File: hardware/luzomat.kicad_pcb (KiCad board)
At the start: 4 copper layers, 187 x 103 mm, 126 parts, among them J1 Screw_Terminal_01x02, J10 Screw_Terminal_01x02, J11 Screw_Terminal_01x02, J12 Screw_Terminal_01x02, J13 Screw_Terminal_01x02, J14 Screw_Terminal_01x02, J15 Screw_Terminal_01x02, J16 Screw_Terminal_01x02, J17 Screw_Terminal_01x02, J18 Screw_Terminal_01x02, J19 Screw_Terminal_01x02, J2 Screw_Terminal_01x02, J20 Screw_Terminal_01x02, J21 Screw_Terminal_01x02, J3 40HAT, J5 Screw_Terminal_01x02, J6 Screw_Terminal_01x02, J7 Screw_Terminal_01x02, J8 Screw_Terminal_01x02, J9 Screw_Terminal_01x02, K1 G5Q-1, K2 G5Q-1, K3 G5Q-1, K4 G5Q-1, K5 G5Q-1, K6 G5Q-1, Q1 DMG2305UX-13, Q10 2N7002, Q11 2N7002, Q12 2N7002, Q13 2N7002, Q2 2N7002, Q3 DMG2305UX-13, Q4 2N7002, Q5 2N7002, Q6 2N7002, Q7 2N7002, Q8 2N7002, Q9 2N7002, U1 CAT24C256, U2 LM1085-3.3, U3 MAX31856, U4 MAX31856, U5 SN74LVC1G123DCTR, U6 SN74LVC1T45DBV

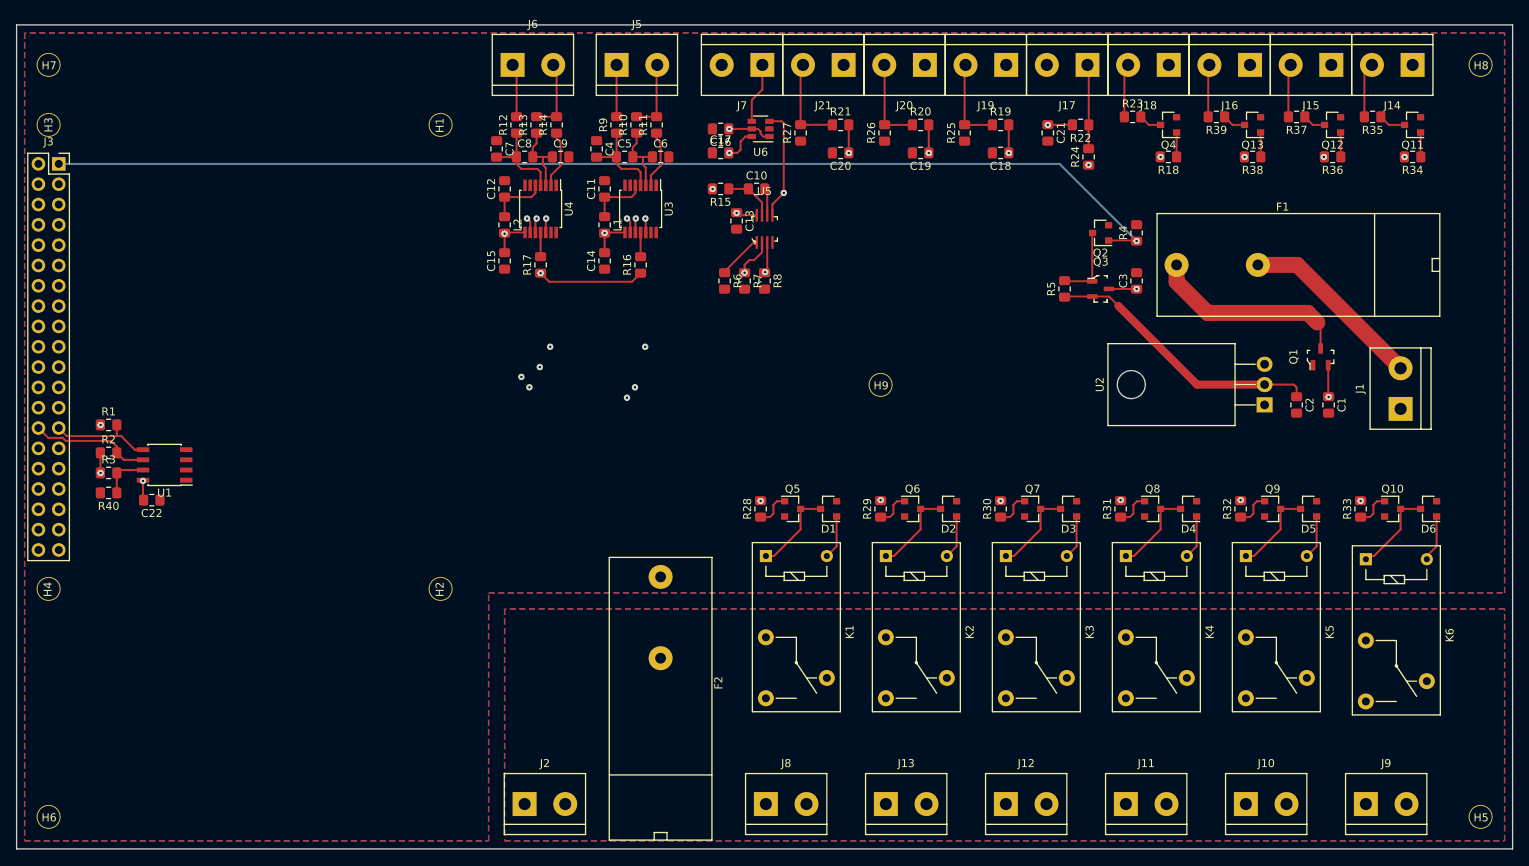
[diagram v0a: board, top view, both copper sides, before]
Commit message: added testpoints and silkscreen
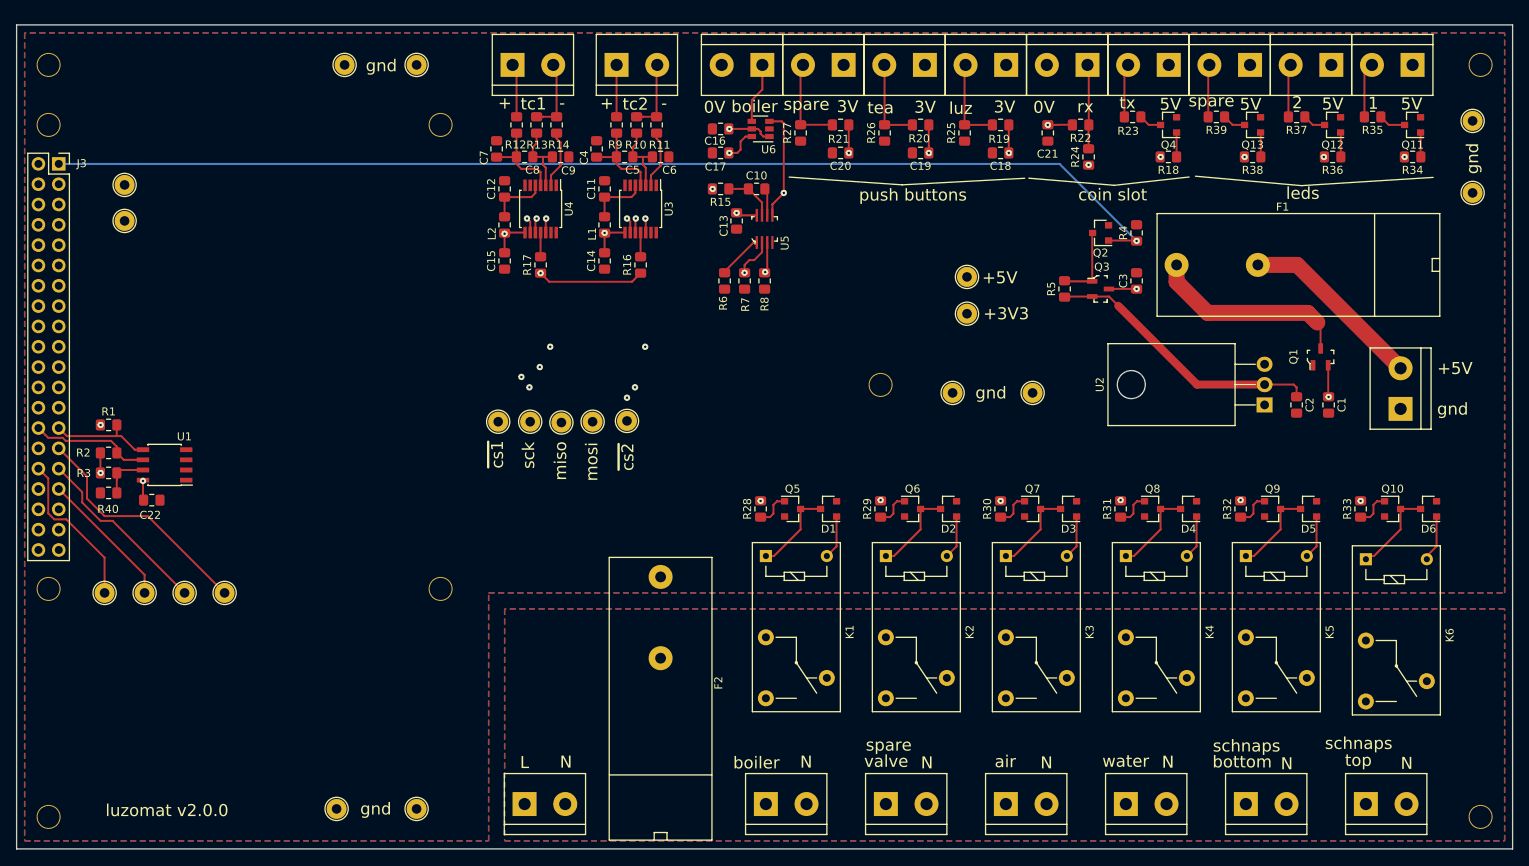
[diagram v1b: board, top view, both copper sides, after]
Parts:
- added TP1: TestPoint, TestPoint:TestPoint_THTPad_D2.5mm_Drill1.2mm, F.Cu at (122.0, 95.6)
- added TP10: TestPoint, TestPoint:TestPoint_THTPad_D2.5mm_Drill1.2mm, F.Cu at (100.0, 51.0)
- added TP11: TestPoint, TestPoint:TestPoint_THTPad_D2.5mm_Drill1.2mm, F.Cu at (91.0, 51.0)
- added TP12: TestPoint, TestPoint:TestPoint_THTPad_D2.5mm_Drill1.2mm, F.Cu at (90.0, 144.0)
- added TP13: TestPoint, TestPoint:TestPoint_THTPad_D2.5mm_Drill1.2mm, F.Cu at (232.0, 67.0)
- added TP16: TestPoint, TestPoint:TestPoint_THTPad_D2.5mm_Drill1.2mm, F.Cu at (110.2, 95.6)
- added TP17: TestPoint, TestPoint:TestPoint_THTPad_D2.5mm_Drill1.2mm, F.Cu at (126.3, 95.5)
- added TP18: TestPoint, TestPoint:TestPoint_THTPad_D2.5mm_Drill1.2mm, F.Cu at (63.5, 66.0)
- added TP19: TestPoint, TestPoint:TestPoint_THTPad_D2.5mm_Drill1.2mm, F.Cu at (63.5, 70.5)
- added TP2: TestPoint, TestPoint:TestPoint_THTPad_D2.5mm_Drill1.2mm, F.Cu at (118.1, 95.7)
- added TP20: TestPoint, TestPoint:TestPoint_THTPad_D2.5mm_Drill1.2mm, F.Cu at (76.0, 117.0)
- added TP21: TestPoint, TestPoint:TestPoint_THTPad_D2.5mm_Drill1.2mm, F.Cu at (71.0, 117.0)
- added TP22: TestPoint, TestPoint:TestPoint_THTPad_D2.5mm_Drill1.2mm, F.Cu at (66.0, 117.0)
- added TP23: TestPoint, TestPoint:TestPoint_THTPad_D2.5mm_Drill1.2mm, F.Cu at (61.0, 117.0)
- added TP3: TestPoint, TestPoint:TestPoint_THTPad_D2.5mm_Drill1.2mm, F.Cu at (114.2, 95.6)
- added TP4: TestPoint, TestPoint:TestPoint_THTPad_D2.5mm_Drill1.2mm, F.Cu at (168.8, 82.1)
- added TP5: TestPoint, TestPoint:TestPoint_THTPad_D2.5mm_Drill1.2mm, F.Cu at (168.8, 77.5)
- added TP6: TestPoint, TestPoint:TestPoint_THTPad_D2.5mm_Drill1.2mm, F.Cu at (100.0, 144.0)
- added TP7: TestPoint, TestPoint:TestPoint_THTPad_D2.5mm_Drill1.2mm, F.Cu at (177.0, 92.0)
- added TP8: TestPoint, TestPoint:TestPoint_THTPad_D2.5mm_Drill1.2mm, F.Cu at (232.0, 58.0)
- added TP9: TestPoint, TestPoint:TestPoint_THTPad_D2.5mm_Drill1.2mm, F.Cu at (167.0, 92.0)
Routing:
- net Net-(J3-Pad29): track 0.00 -> 29.8 mm
- net Net-(J3-Pad31): track 0.00 -> 22.9 mm
- net Net-(J3-Pad32): track 0.00 -> 19.8 mm
- net Net-(J3-Pad33): track 0.00 -> 17.4 mm
- net /mosi: track 109.1 -> 120.7 mm
- net Net-(J3-Pad5): track 0.00 -> 9.08 mm
- net Net-(J3-Pad3): track 0.00 -> 8.27 mm
- net /miso: track 85.3 -> 93.4 mm
- net /~cs1: track 82.9 -> 89.7 mm
- net /sck: track 118.2 -> 122.6 mm
- net /~cs2: track 98.4 -> 101.3 mm
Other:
- board text added: "+"
- board text added: "+3V3"
- board text added: "+5V"
- board text added: "-"
- board text added: "0V"
- board text added: "1"
- board text added: "2"
- board text added: "3V"
- board text added: "5V"
- board text added: "L"
- board text added: "N"
- board text added: "air"
- board text added: "boiler"
- board text added: "bottom"
- board text added: "coin slot"
- board text added: "gnd"
- board text added: "leds"
- board text added: "luz"
- board text added: "luzomat v2.0.0"
- board text added: "miso"
- board text added: "mosi"
- board text added: "push buttons"
- board text added: "rx"
- board text added: "schnaps"
- board text added: "sck"
- board text added: "spare"
- board text added: "tc1"
- board text added: "tc2"
- board text added: "tea"
- board text added: "top"
- board text added: "tx"
- board text added: "valve"
- board text added: "water"
- board text added: "~cs1"
- board text added: "~cs2"

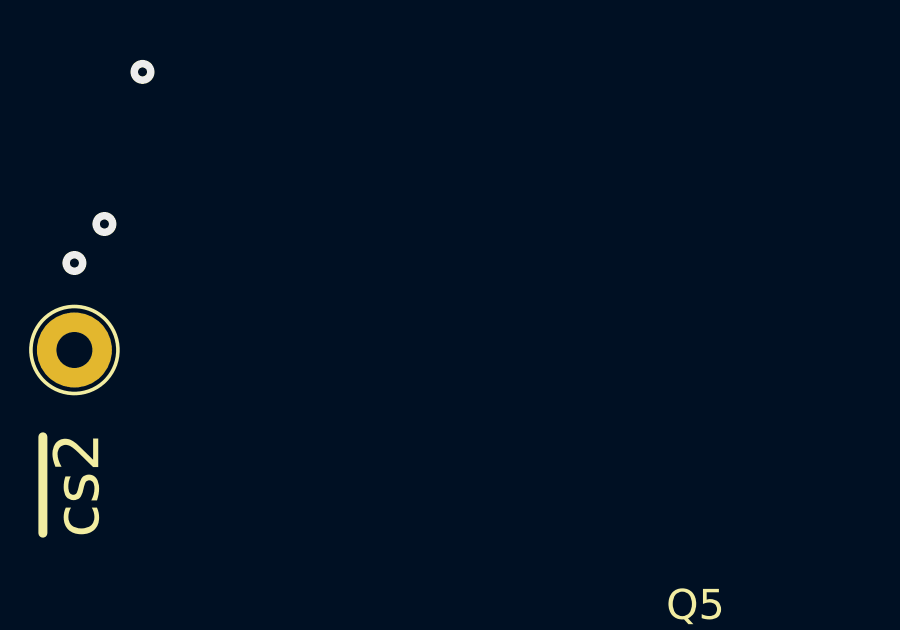
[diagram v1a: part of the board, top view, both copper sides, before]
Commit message: added skier, ordered pcb
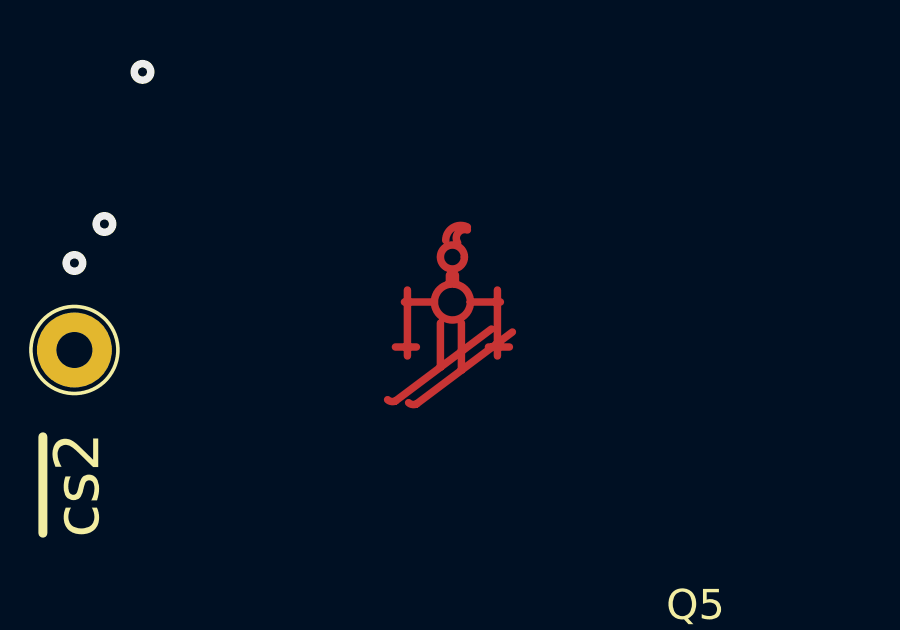
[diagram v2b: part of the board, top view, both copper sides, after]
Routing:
- net (no net): track 0.00 -> 34.9 mm
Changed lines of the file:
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@@
   (general
     (thickness 1.6)
-    (drawings 82)
-    (tracks 484)
+    (drawings 106)
+    (tracks 507)
     (zones 0)
     (modules 147)
@@
     (36 B.SilkS user hide)
     (37 F.SilkS user)
-    (38 B.Mask user hide)
-    (39 F.Mask user hide)
-    (40 Dwgs.User user hide)
+    (38 B.Mask user)
+    (39 F.Mask user)
+    (40 Dwgs.User user)
     (41 Cmts.User user hide)
     (42 Eco1.User user hide)
@@
     (44 Edge.Cuts user)
     (45 Margin user)
-    (46 B.CrtYd user hide)
+    (46 B.CrtYd user)
     (47 F.CrtYd user)
     (48 B.Fab user hide)
@@
   )
   (setup
-    (last_trace_width 0.25)
+    (last_trace_width 0.5)
     (user_trace_width 0.15)
     (user_trace_width 0.2)
@@
     (user_trace_width 2)
     (trace_clearance 0.25)
-    (zone_clearance 0.25)
+    (zone_clearance 0.2)
     (zone_45_only no)
     (trace_min 0.15)
-    (segment_width 0.15)
+    (segment_width 0.5)
     (edge_width 0.15)
     (via_size 0.8)
@@
     (visible_elements 7FFFFE3F)
     (pcbplotparams
-      (layerselection 0x010f8_80000007)
+      (layerselection 0x011e0_ffffffff)
       (usegerberextensions false)
-      (usegerberattributes false)
-      (usegerberadvancedattributes false)
-      (creategerberjobfile false)
+      (usegerberattributes true)
+      (usegerberadvancedattributes true)
+      (creategerberjobfile true)
       (excludeedgelayer false)
       (linewidth 0.100000)
       (plotframeref false)
-      (viasonmask false)
+      (viasonmask true)
       (mode 1)
       (useauxorigin false)
@@
       (psnegative false)
       (psa4output false)
-      (plotreference true)
+      (plotreference false)
       (plotvalue false)
       (plotinvisibletext false)
@@
       (clearance 1.6))
   )
+  (gr_line (start 140.91 94.89) (end 137.79 97.22) (layer F.Mask) (width 0.5))
+  (gr_line (start 140.3 94.74) (end 137.16 97.09) (layer F.Mask) (width 0.5))
+  (gr_line (start 139.2 94.47) (end 139.19 96.18) (layer F.Mask) (width 0.5))
+  (gr_line (start 138.5 94.49) (end 138.51 96.02) (layer F.Mask) (width 0.5))
+  (gr_line (start 139.46 93.9) (end 140.35 93.9) (layer F.Mask) (width 0.5))
+  (gr_line (start 137.48 93.88) (end 138.31 93.88) (layer F.Mask) (width 0.5))
+  (gr_line (start 136.98 95.39) (end 137.72 95.39) (layer F.Mask) (width 0.5))
+  (gr_line (start 137.4 93.49) (end 137.4 95.7) (layer F.Mask) (width 0.5))
+  (gr_line (start 140.075 95.4) (end 140.8 95.4) (layer F.Mask) (width 0.5))
+  (gr_line (start 140.4 93.5) (end 140.4 95.7) (layer F.Mask) (width 0.5))
+  (gr_line (start 138.8 92.99) (end 138.8 93.31) (layer F.Mask) (width 0.5))
+  (gr_line (start 139 92.99) (end 139 93.31) (layer F.Mask) (width 0.5))
+  (gr_arc (start 137.60448 97.04397) (end 137.43879 97.23118) (angle -64) (layer F.Mask) (width 0.5))
+  (gr_arc (start 136.90448 96.94396) (end 136.73879 97.13117) (angle -64) (layer F.Mask) (width 0.5))
+  (gr_arc (start 138.89999 93.9) (end 139.49999 93.9) (angle -360) (layer F.Mask) (width 0.5))
+  (gr_arc (start 138.89999 92.4) (end 139.29999 92.4) (angle -360) (layer F.Mask) (width 0.5))
+  (gr_arc (start 139.17639 91.84721) (end 139.4 91.4) (angle -116.565) (layer F.Mask) (width 0.5))
+  (gr_arc (start 139.31055 91.76833) (end 139.39999 91.5) (angle -142.125) (layer F.Mask) (width 0.5))
+  (gr_arc (start 136.90448 96.96896) (end 136.73879 97.15617) (angle -63.9732098) (layer F.Cu) (width 0.25))
+  (gr_arc (start 137.60448 97.06897) (end 137.43879 97.25618) (angle -63.9732098) (layer F.Cu) (width 0.25))
+  (gr_arc (start 139.17639 91.84721) (end 139.4 91.4) (angle -116.565) (layer F.Cu) (width 0.25))
+  (gr_arc (start 139.31055 91.76833) (end 139.39999 91.5) (angle -142.125) (layer F.Cu) (width 0.25))
+  (gr_arc (start 138.89999 92.4) (end 139.29999 92.4) (angle -360) (layer F.Cu) (width 0.25))
+  (gr_arc (start 138.89999 93.9) (end 139.49999 93.9) (angle -360) (layer F.Cu) (width 0.25))
   (gr_text "luzomat v2.0.0" (at 68.8 144.2) (layer F.SilkS)
     (effects (font (size 1.5 1.5) (thickness 0.3)))
@@
   (gr_line (start 50.5 58) (end 50.5 137) (layer F.CrtYd) (width 0.1))
   (gr_arc (start 53.5 137) (end 53.5 140) (angle 90) (layer F.CrtYd) (width 0.1))
+  (segment (start 139.5 93.9) (end 140.49999 93.9) (width 0.25) (layer F.Cu) (net 0))
+  (segment (start 140.39999 95.7) (end 140.39999 93.5) (width 0.25) (layer F.Cu) (net 0))
+  (segment (start 140.1 95.4) (end 140.8 95.4) (width 0.25) (layer F.Cu) (net 0))
+  (segment (start 137 95.4) (end 137.7 95.4) (width 0.25) (layer F.Cu) (net 0))
+  (segment (start 137.4 95.7) (end 137.4 93.5) (width 0.25) (layer F.Cu) (net 0))
+  (segment (start 137.3 93.9) (end 138.3 93.9) (width 0.25) (layer F.Cu) (net 0))
+  (segment (start 139 93.3) (end 139 93) (width 0.25) (layer F.Cu) (net 0))
+  (segment (start 138.8 93.3) (end 138.8 93) (width 0.25) (layer F.Cu) (net 0))
+  (segment (start 137.69999 97.3) (end 140.9 94.9) (width 0.25) (layer F.Cu) (net 0))
+  (segment (start 139.19935 96.17549) (end 139.20004 94.6) (width 0.25) (layer F.Cu) (net 0))
+  (segment (start 138.49935 96.07548) (end 138.5 94.6) (width 0.25) (layer F.Cu) (net 0))
+  (segment (start 137 97.2) (end 140.2 94.8) (width 0.25) (layer F.Cu) (net 0))
+  (segment (start 139.5 93.9) (end 140.49999 93.9) (width 0.5) (layer F.Mask) (net 0))
+  (segment (start 140.39999 95.7) (end 140.39999 93.5) (width 0.5) (layer F.Mask) (net 0))
+  (segment (start 140.1 95.4) (end 140.8 95.4) (width 0.5) (layer F.Mask) (net 0))
+  (segment (start 137 95.4) (end 137.7 95.4) (width 0.5) (layer F.Mask) (net 0))
+  (segment (start 137.4 95.7) (end 137.4 93.5) (width 0.5) (layer F.Mask) (net 0))
+  (segment (start 137.3 93.9) (end 138.3 93.9) (width 0.5) (layer F.Mask) (net 0))
+  (segment (start 139 93.3) (end 139 93) (width 0.5) (layer F.Mask) (net 0))
+  (segment (start 138.8 93.3) (end 138.8 93) (width 0.5) (layer F.Mask) (net 0))
+  (segment (start 139.19935 96.17549) (end 139.20004 94.6) (width 0.5) (layer F.Mask) (net 0))
+  (segment (start 138.49935 96.07548) (end 138.5 94.6) (width 0.5) (layer F.Mask) (net 0))
+  (segment (start 137 97.2) (end 140.2 94.8) (width 0.5) (layer F.Mask) (net 0))
   (segment (start 63.41 65.91) (end 63.5 66) (width 0.25) (layer In1.Cu) (net 2))
   (segment (start 55.27 65.91) (end 63.41 65.91) (width 0.25) (layer In1.Cu) (net 2))
@@
     )
   )
-  (zone (net 9) (net_name +3V3) (layer In1.Cu) (hatch edge 0.508)
+  (zone (net 12) (net_name +5V) (layer In2.Cu) (hatch edge 0.508)
     (connect_pads (clearance 0.25))
     (min_thickness 0.15)
@@
     )
   )
-  (zone (net 12) (net_name +5V) (layer In2.Cu) (hatch edge 0.508)
+  (zone (net 1) (net_name GND) (layer B.Cu) (hatch edge 0.508)
     (connect_pads (clearance 0.25))
     (min_thickness 0.15)
@@
     )
   )
-  (zone (net 1) (net_name GND) (layer B.Cu) (hatch edge 0.508)
+  (zone (net 0) (net_name "") (layers F.Cu In1.Cu In2.Cu B.Cu) (hatch edge 0.508)
+    (connect_pads (clearance 0.2))
+    (min_thickness 0.254)
+    (keepout (tracks allowed) (vias allowed) (copperpour not_allowed))
+    (fill (arc_segments 16) (thermal_gap 0.508) (thermal_bridge_width 0.508))
+    (polygon
+      (pts
+        (xy 126.5 111.5) (xy 134.5 111.5) (xy 134.5 118.5) (xy 126.5 118.5)
+      )
+    )
+  )
+  (zone (net 9) (net_name +3V3) (layer In1.Cu) (hatch edge 0.508)
     (connect_pads (clearance 0.25))
     (min_thickness 0.15)
